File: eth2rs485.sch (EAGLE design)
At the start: 61 parts, among them IC1 VREG-OKI-78SR-5.0/1.5-W36, IC2 MAX485, IC3 24AA025E48, Q1 16MHz, T1 74990101217, U1 AP2210K, U2 ATMEGA328P-AU, U3 W5500, Y1 IT-L30-010

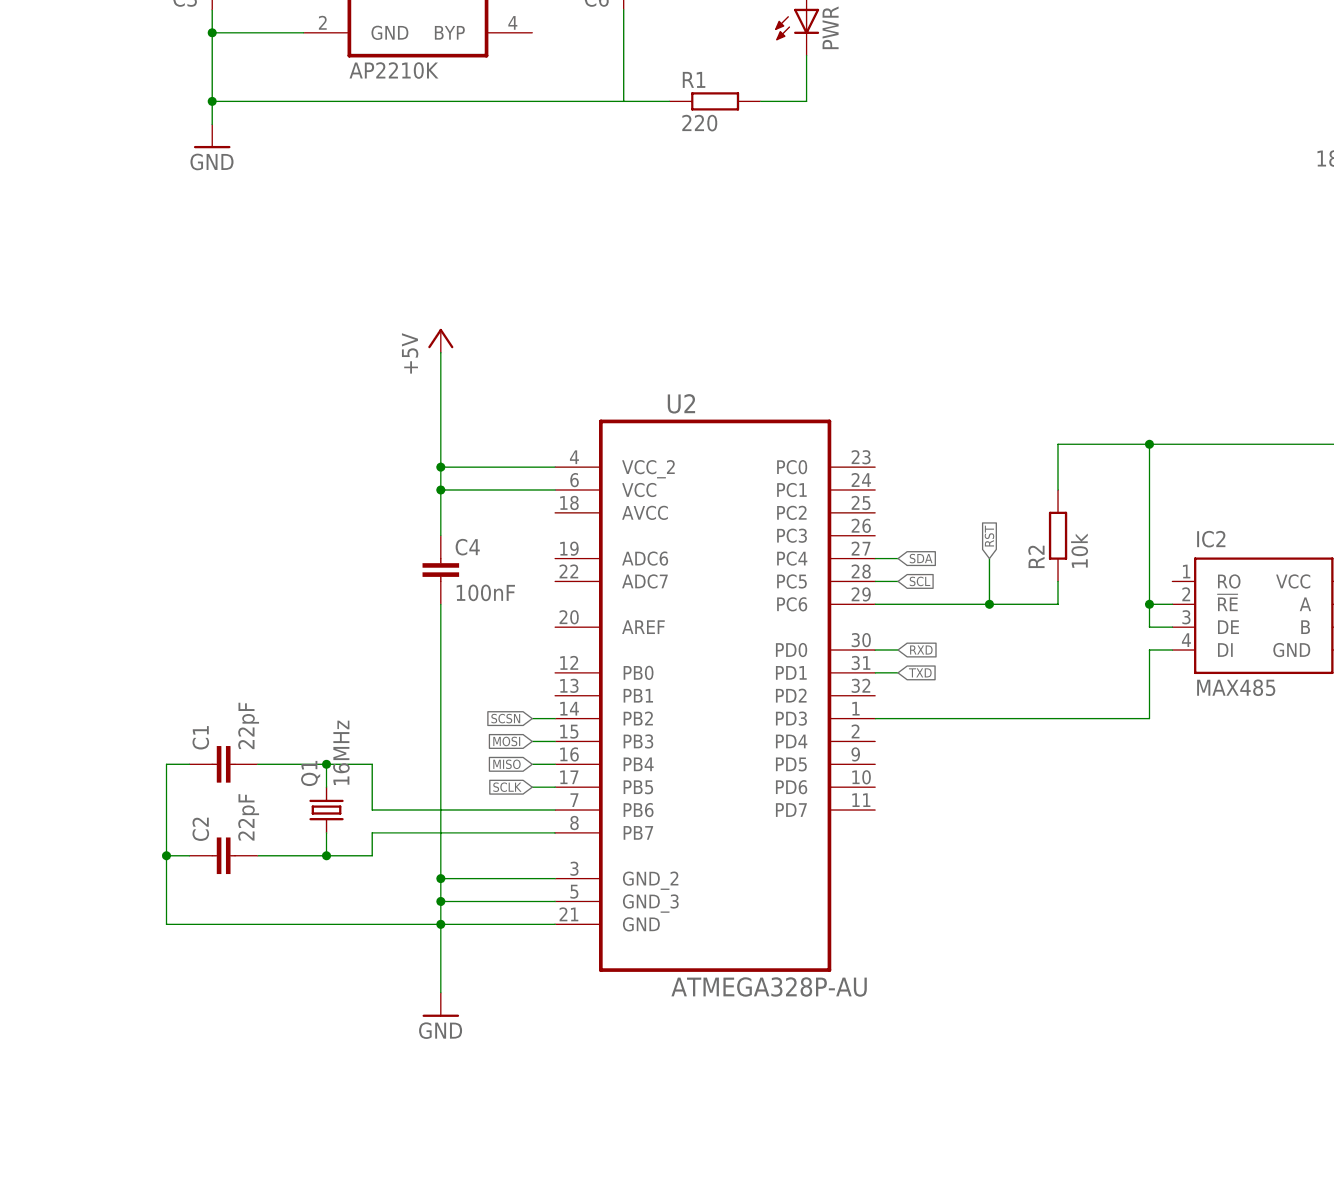
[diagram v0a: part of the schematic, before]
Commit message: swapped 328p for 644p
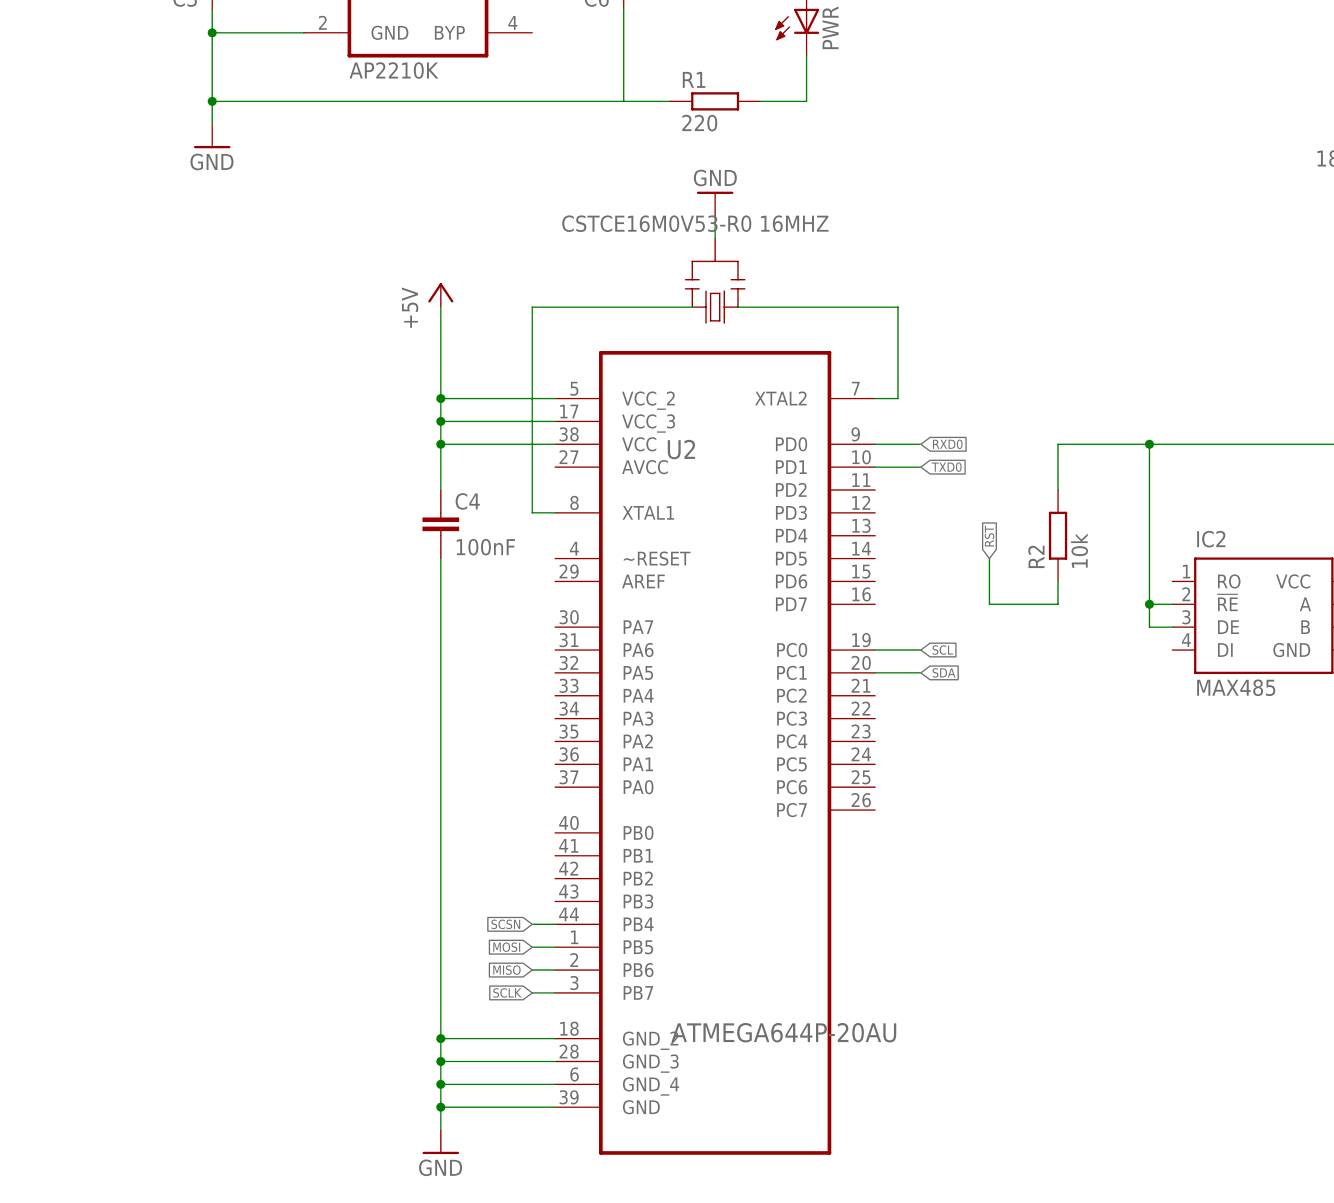
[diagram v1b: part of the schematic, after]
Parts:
- removed C1, C2: 22pF, rcl:C-EUC0805
- removed Q1: 16MHz, adafruit:CRYSTALHC49U70
- added Y2: CSTCE16M0V53-R0 16MHZ, SmartPrj:RESONATORMU
- U2: value ATMEGA328P-AU -> ATMEGA644P-20AU; device Atmel_By_element14_Batch_1-00:ATMEGA328P-AU -> Atmel_By_element14_Batch_1-00:ATMEGA644P-20AU
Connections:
- removed net DOUT: IC2.DI, U2.PD3
- new net RXD0: U2.PD0
- new net TXD0: U2.PD1
- net +5V: now also U2.VCC_3
- net GND: now also U2.GND_4, Y2.2; no longer C1.1, C2.1
- net MISO: now also U2.PB6; no longer U2.PB4
- net MOSI: now also U2.PB5; no longer U2.PB3
- net N$2: now also U2.XTAL1, Y2.3; no longer C2.2, Q1.1, U2.PB7
- net N$3: now also U2.XTAL2, Y2.1; no longer C1.2, Q1.2, U2.PB6
- net RST: no longer U2.PC6
- net RXD: no longer U2.PD0
- net SCL: now also U2.PC0; no longer U2.PC5
- net SCLK: now also U2.PB7; no longer U2.PB5
- net SCSN: now also U2.PB4; no longer U2.PB2
- net SDA: now also U2.PC1; no longer U2.PC4
- net TXD: no longer U2.PD1
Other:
- moved on the sheet: C4

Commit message: finished routing for prototype
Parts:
- removed R14, R15, R16, R17: 33R, rcl:R-EU_R0805
- added R6: 10k, rcl:R-EU_R0805
- U1: value AP2210K -> AP2112
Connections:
- net N$2 renamed XTAL1
- net N$3 renamed XTAL2
- removed net N$20: R16.2, U3.RXP
- removed net N$26: R17.2, U3.RXN
- removed net N$27: R14.2, U3.TXP
- removed net N$28: R15.2, U3.TXN
- removed net RXD: JP3.2
- removed net TXD: JP3.3
- new net 485MODE: IC2.!RE, IC2.DE, U2.PD6
- new net N$2: R6.1, U1.EN
- new net RXD1: IC2.RO, U2.PD2
- new net TXD1: IC2.DI, U2.PD3
- net +5V: now also R6.2, U2.AVCC; no longer IC2.!RE, IC2.DE, U1.EN
- net RST: now also U2.~RESET
- net RXD0: now also JP3.2
- net RXN: now also U3.RXN; no longer R17.1
- net RXP: now also U3.RXP; no longer R16.1
- net TXD0: now also JP3.3
- net TXN: now also U3.TXN; no longer R15.1
- net TXP: now also U3.TXP; no longer R14.1
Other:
- note added: "Ethernet RS485 Bridge V0.1 codm.de 2019 CC-BY-SA"
- note removed: "Ethernet DMX Bridge V0.4 codm.de 2018 CC-BY-SA"
- moved on the sheet: C4, R2

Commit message: atmega 644 working (hopefully)
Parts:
- C3: value 1µF -> 10uF
- C6: value 2.2µF -> 10uF
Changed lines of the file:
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@@
 <?xml version="1.0" encoding="utf-8"?>
 <!DOCTYPE eagle SYSTEM "eagle.dtd">
-<eagle version="9.3.0">
+<eagle version="9.3.1">
 <drawing>
 <settings>
@@
 <part name="C12" library="rcl" library_urn="urn:adsk.eagle:library:334" deviceset="C-EU" device="C0805" package3d_urn="urn:adsk.eagle:package:23617/2" value="4.7uF"/>
 <part name="Y1" library="IT-L30-010" deviceset="IT-L30-010" device=""/>
-<part name="C3" library="rcl" library_urn="urn:adsk.eagle:library:334" deviceset="C-EU" device="C0805" package3d_urn="urn:adsk.eagle:package:23617/2" value="1µF"/>
-<part name="C6" library="rcl" library_urn="urn:adsk.eagle:library:334" deviceset="C-EU" device="C0805" package3d_urn="urn:adsk.eagle:package:23617/2" value="2.2µF"/>
+<part name="C3" library="rcl" library_urn="urn:adsk.eagle:library:334" deviceset="C-EU" device="C0805" package3d_urn="urn:adsk.eagle:package:23617/2" value="10uF"/>
+<part name="C6" library="rcl" library_urn="urn:adsk.eagle:library:334" deviceset="C-EU" device="C0805" package3d_urn="urn:adsk.eagle:package:23617/2" value="10uF"/>
 <part name="U1" library="diodes-inc" deviceset="AP2210" device="K" value="AP2112"/>
 <part name="+3V31" library="supply1" deviceset="+3V3" device=""/>

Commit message: added sch pdf, minor changes brd
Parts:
- C10, C13: value 0.1uF -> 100nF
- C15: device rcl:R-EU_R0805 -> rcl:C-EUC0805
- R1: value 220 -> 2k7
- X1: value (none) -> MSTBA3; device con-ptr500:AK500/3 -> con-phoenix-508:MSTBA3
- X2: value (none) -> MSTBA2; device con-ptr500:AK500/2 -> con-phoenix-508:MSTBA2
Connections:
- net GND: now also X2-1.1; no longer X2-1.KL
- net N$4: now also X1-1.1; no longer X1-1.KL
- net N$5: now also X1-3.1; no longer X1-3.KL
- net N$6: now also X1-2.1; no longer X1-2.KL
- net VCC: now also X2-2.1; no longer X2-2.KL
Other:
- note added: "Ethernet RS485 Bridge V0.3 codm.de 2020 CC-BY-NC-SA"
- note removed: "Ethernet RS485 Bridge V0.1 codm.de 2019 CC-BY-SA"
- moved on the sheet: C15
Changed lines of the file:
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@@
 <?xml version="1.0" encoding="utf-8"?>
 <!DOCTYPE eagle SYSTEM "eagle.dtd">
-<eagle version="9.3.1">
+<eagle version="9.6.2">
 <drawing>
 <settings>
@@
 <part name="C8" library="rcl" library_urn="urn:adsk.eagle:library:334" deviceset="C-EU" device="C0805" package3d_urn="urn:adsk.eagle:package:23617/2" value="18pF"/>
 <part name="C7" library="rcl" library_urn="urn:adsk.eagle:library:334" deviceset="C-EU" device="C0805" package3d_urn="urn:adsk.eagle:package:23617/2" value="18pF"/>
-<part name="C10" library="rcl" library_urn="urn:adsk.eagle:library:334" deviceset="C-EU" device="C0805" package3d_urn="urn:adsk.eagle:package:23617/2" value="0.1uF"/>
+<part name="C10" library="rcl" library_urn="urn:adsk.eagle:library:334" deviceset="C-EU" device="C0805" package3d_urn="urn:adsk.eagle:package:23617/2" value="100nF"/>
 <part name="C11" library="rcl" library_urn="urn:adsk.eagle:library:334" deviceset="C-EU" device="C0805" package3d_urn="urn:adsk.eagle:package:23617/2" value="10nF"/>
 <part name="C16" library="rcl" library_urn="urn:adsk.eagle:library:334" deviceset="C-EU" device="C0805" package3d_urn="urn:adsk.eagle:package:23617/2" value="10nF"/>
@@
 <part name="C18" library="rcl" library_urn="urn:adsk.eagle:library:334" deviceset="C-EU" device="C0805" package3d_urn="urn:adsk.eagle:package:23617/2" value="6.8nF"/>
 <part name="C19" library="rcl" library_urn="urn:adsk.eagle:library:334" deviceset="C-EU" device="C0805" package3d_urn="urn:adsk.eagle:package:23617/2" value="22nF"/>
-<part name="C13" library="rcl" library_urn="urn:adsk.eagle:library:334" deviceset="C-EU" device="C0805" package3d_urn="urn:adsk.eagle:package:23617/2" value="0.1uF"/>
+<part name="C13" library="rcl" library_urn="urn:adsk.eagle:library:334" deviceset="C-EU" device="C0805" package3d_urn="urn:adsk.eagle:package:23617/2" value="100nF"/>
 <part name="C9" library="CAP" deviceset="C-3216(TANTAL)" device="" value="10uF/16V"/>
 <part name="C14" library="CAP" deviceset="C-3216(TANTAL)" device="" value="10uF/16V"/>
@@
 <part name="P+1" library="supply1" deviceset="+5V" device=""/>
 <part name="T1" library="SignalCommunications (rev17d)" deviceset="WE-RJ45_74990111217" device="" value="74990101217"/>
-<part name="X1" library="con-ptr500" library_urn="urn:adsk.eagle:library:181" deviceset="AK500/3" device="" package3d_urn="urn:adsk.eagle:package:9883/1"/>
-<part name="X2" library="con-ptr500" library_urn="urn:adsk.eagle:library:181" deviceset="AK500/2" device="" package3d_urn="urn:adsk.eagle:package:9880/1"/>
+<part name="X1" library="con-phoenix-508" library_urn="urn:adsk.eagle:library:176" deviceset="MSTBA3" device="" package3d_urn="urn:adsk.eagle:package:9608/1"/>
+<part name="X2" library="con-phoenix-508" library_urn="urn:adsk.eagle:library:176" deviceset="MSTBA2" device="" package3d_urn="urn:adsk.eagle:package:9615/1"/>
 <part name="R9" library="rcl" library_urn="urn:adsk.eagle:library:334" deviceset="R-EU_" device="R0805" package3d_urn="urn:adsk.eagle:package:23553/2" value="120"/>
 <part name="JP1" library="jumper" library_urn="urn:adsk.eagle:library:252" deviceset="JP1Q" device="" package3d_urn="urn:adsk.eagle:package:15455/1"/>
@@
 <part name="P+7" library="supply1" deviceset="+5V" device=""/>
 <part name="GND11" library="supply1" deviceset="GND" device=""/>
-<part name="C15" library="rcl" library_urn="urn:adsk.eagle:library:334" deviceset="R-EU_" device="R0805" package3d_urn="urn:adsk.eagle:package:23553/2" value="100nF"/>
+<part name="C15" library="rcl" library_urn="urn:adsk.eagle:library:334" deviceset="C-EU" device="C0805" package3d_urn="urn:adsk.eagle:package:23617/2" value="100nF"/>
 <part name="R5" library="rcl" library_urn="urn:adsk.eagle:library:334" deviceset="R-EU_" device="R0805" package3d_urn="urn:adsk.eagle:package:23553/2" value="100"/>
 <part name="R4" library="rcl" library_urn="urn:adsk.eagle:library:334" deviceset="R-EU_" device="R0805" package3d_urn="urn:adsk.eagle:package:23553/2" value="4,7"/>
@@
 <part name="+3V36" library="supply1" deviceset="+3V3" device=""/>
 <part name="LOGO1" library="SparkFun-Aesthetics" deviceset="OSHW-LOGO" device="M" value="OSHW-LOGOM"/>
-<part name="R1" library="rcl" library_urn="urn:adsk.eagle:library:334" deviceset="R-EU_" device="R0805" package3d_urn="urn:adsk.eagle:package:23553/2" value="220"/>
+<part name="R1" library="rcl" library_urn="urn:adsk.eagle:library:334" deviceset="R-EU_" device="R0805" package3d_urn="urn:adsk.eagle:package:23553/2" value="2k7"/>
 <part name="PWR" library="led" library_urn="urn:adsk.eagle:library:259" deviceset="LED" device="CHIP-LED0805" package3d_urn="urn:adsk.eagle:package:15818/2"/>
 <part name="D2" library="diode" library_urn="urn:adsk.eagle:library:210" deviceset="DIODE-2CA|AC" device="SOT23" package3d_urn="urn:adsk.eagle:package:43389/2" value="SM712"/>
@@
 <sheet>
 <plain>
-<text x="200.66" y="38.1" size="5.08" layer="91" font="vector" align="center">Ethernet RS485 Bridge V0.1
-codm.de 2019
-CC-BY-SA
+<text x="200.66" y="38.1" size="5.08" layer="91" font="vector" align="center">Ethernet RS485 Bridge V0.3
+codm.de 2020
+CC-BY-NC-SA
 </text>
 </plain>
@@
 <attribute name="VALUE" x="269.24" y="43.18" size="1.778" layer="96"/>
 </instance>
-<instance part="C15" gate="G$1" x="325.12" y="58.42" smashed="yes" rot="R270">
-<attribute name="NAME" x="326.6186" y="62.23" size="1.778" layer="95" rot="R270"/>
-<attribute name="VALUE" x="321.818" y="62.23" size="1.778" layer="96" rot="R270"/>
+<instance part="C15" gate="G$1" x="325.12" y="60.96" smashed="yes">
+<attribute name="NAME" x="321.31" y="62.4586" size="1.778" layer="95"/>
+<attribute name="VALUE" x="321.31" y="57.658" size="1.778" layer="96"/>
 </instance>
 <instance part="R5" gate="G$1" x="124.46" y="195.58" smashed="yes" rot="R90">
@@
 <segment>
 <pinref part="GND6" gate="1" pin="GND"/>
-<pinref part="X2" gate="-1" pin="KL"/>
+<pinref part="X2" gate="-1" pin="1"/>
 <wire x1="149.86" y1="190.5" x2="149.86" y2="205.74" width="0.1524" layer="91"/>
 </segment>
@@
 <wire x1="144.78" y1="182.88" x2="144.78" y2="195.58" width="0.1524" layer="91"/>
 <pinref part="P+5" gate="VCC" pin="VCC"/>
-<pinref part="X2" gate="-2" pin="KL"/>
+<pinref part="X2" gate="-2" pin="1"/>
 <wire x1="144.78" y1="195.58" x2="144.78" y2="198.12" width="0.1524" layer="91"/>
 <wire x1="144.78" y1="198.12" x2="144.78" y2="205.74" width="0.1524" layer="91"/>
@@
 <segment>
 <pinref part="C15" gate="G$1" pin="2"/>
-<wire x1="325.12" y1="53.34" x2="325.12" y2="50.8" width="0.1524" layer="91"/>
+<wire x1="325.12" y1="55.88" x2="325.12" y2="50.8" width="0.1524" layer="91"/>
 <label x="325.12" y="50.8" size="1.4224" layer="95" rot="R270" xref="yes"/>
 </segment>
@@
 <net name="N$4" class="0">
 <segment>
-<pinref part="X1" gate="-1" pin="KL"/>
+<pinref part="X1" gate="-1" pin="1"/>
 <pinref part="R5" gate="G$1" pin="2"/>
 <wire x1="124.46" y1="205.74" x2="124.46" y2="200.66" width="0.1524" layer="91"/>
@@
 <net name="N$5" class="0">
 <segment>
-<pinref part="X1" gate="-3" pin="KL"/>
+<pinref part="X1" gate="-3" pin="1"/>
 <pinref part="R3" gate="G$1" pin="2"/>
 <wire x1="114.3" y1="205.74" x2="114.3" y2="200.66" width="0.1524" layer="91"/>
@@
 <net name="N$6" class="0">
 <segment>
-<pinref part="X1" gate="-2" pin="KL"/>
+<pinref part="X1" gate="-2" pin="1"/>
 <pinref part="R4" gate="G$1" pin="2"/>
 <wire x1="119.38" y1="205.74" x2="119.38" y2="193.04" width="0.1524" layer="91"/>
